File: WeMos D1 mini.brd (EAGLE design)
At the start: 25.4 x 28.9 mm, 19 parts

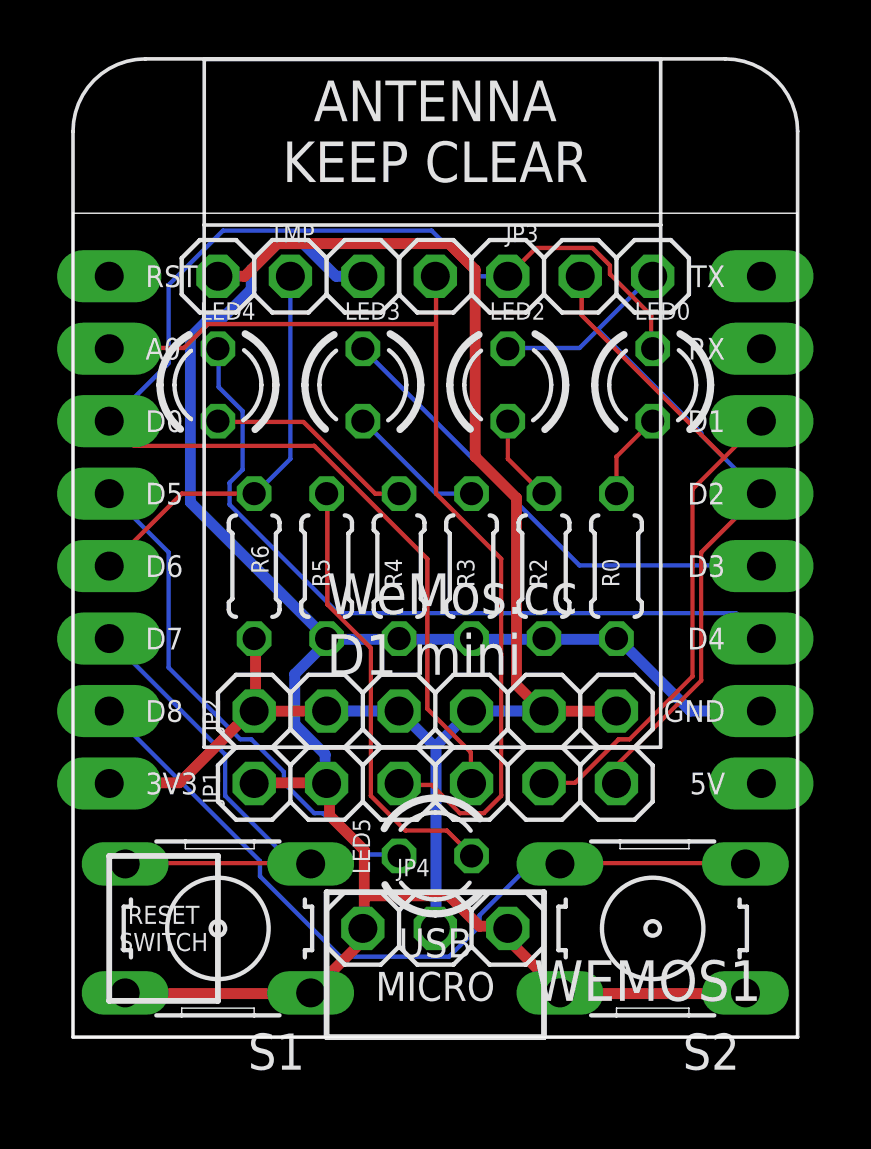
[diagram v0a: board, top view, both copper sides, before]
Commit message: Changed esp8266modules.lbr (esthetics)
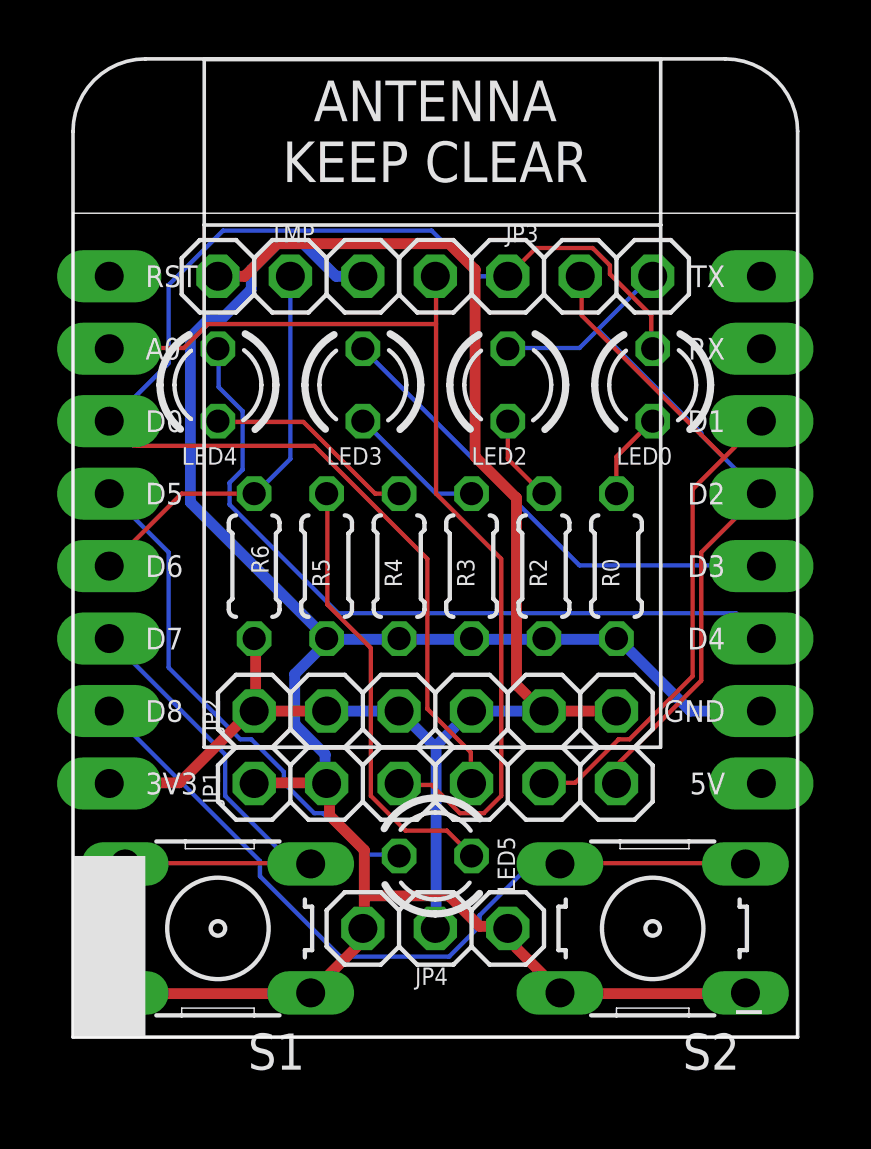
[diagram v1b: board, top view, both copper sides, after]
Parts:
- renumbered WEMOS1 to _
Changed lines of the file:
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@@
 </autorouter>
 <elements>
-<element name="WEMOS1" library="esp8266modules" package="WEMOS-D1-MINI" value="" x="11.43" y="19.05" smashed="yes">
+<element name="_" library="esp8266modules" package="WEMOS-D1-MINI" value="" x="11.43" y="19.05" smashed="yes">
 <attribute name="NAME" x="24.13" y="1.27" size="1.4224" layer="25" align="bottom-right"/>
 </element>
@@
 </element>
 <element name="LED0" library="led" library_urn="urn:adsk.eagle:library:259" package="LED3MM" package3d_urn="urn:adsk.eagle:package:15797/1" value="" x="20.32" y="22.86" smashed="yes" rot="R270">
-<attribute name="NAME" x="19.685" y="25.146" size="0.6096" layer="25" ratio="10"/>
+<attribute name="NAME" x="19.05" y="20.066" size="0.6096" layer="25" ratio="10"/>
 <attribute name="VALUE" x="18.669" y="20.955" size="1.27" layer="27" ratio="10" rot="R270"/>
 </element>
 <element name="LED2" library="led" library_urn="urn:adsk.eagle:library:259" package="LED3MM" package3d_urn="urn:adsk.eagle:package:15797/1" value="" x="15.24" y="22.86" smashed="yes" rot="R270">
-<attribute name="NAME" x="14.605" y="25.146" size="0.6096" layer="25" ratio="10"/>
+<attribute name="NAME" x="13.97" y="20.066" size="0.6096" layer="25" ratio="10"/>
 <attribute name="VALUE" x="13.589" y="20.955" size="1.27" layer="27" ratio="10" rot="R270"/>
 </element>
 <element name="LED3" library="led" library_urn="urn:adsk.eagle:library:259" package="LED3MM" package3d_urn="urn:adsk.eagle:package:15797/1" value="" x="10.16" y="22.86" smashed="yes" rot="R270">
-<attribute name="NAME" x="9.525" y="25.146" size="0.6096" layer="25" ratio="10"/>
+<attribute name="NAME" x="8.89" y="20.066" size="0.6096" layer="25" ratio="10"/>
 <attribute name="VALUE" x="8.509" y="20.955" size="1.27" layer="27" ratio="10" rot="R270"/>
 </element>
@@
 </element>
 <element name="LED4" library="led" library_urn="urn:adsk.eagle:library:259" package="LED3MM" package3d_urn="urn:adsk.eagle:package:15797/1" value="" x="5.08" y="22.86" smashed="yes" rot="R270">
-<attribute name="NAME" x="4.445" y="25.146" size="0.6096" layer="25" ratio="10"/>
+<attribute name="NAME" x="3.81" y="20.066" size="0.6096" layer="25" ratio="10"/>
 <attribute name="VALUE" x="3.429" y="20.955" size="1.27" layer="27" ratio="10" rot="R270"/>
 </element>
@@
 </element>
 <element name="LED5" library="led" library_urn="urn:adsk.eagle:library:259" package="LED3MM" package3d_urn="urn:adsk.eagle:package:15797/1" value="" x="12.7" y="6.35" smashed="yes">
-<attribute name="NAME" x="10.414" y="5.715" size="0.6096" layer="25" ratio="10" rot="R90"/>
+<attribute name="NAME" x="15.494" y="5.08" size="0.6096" layer="25" ratio="10" rot="R90"/>
 <attribute name="VALUE" x="14.605" y="4.699" size="1.27" layer="27" ratio="10"/>
 </element>
@@
 </element>
 <element name="JP4" library="pinhead_v2" package="1X03/OCT" value="" x="12.7" y="3.81" smashed="yes">
-<attribute name="NAME" x="11.3538" y="5.6388" size="0.6096" layer="25" ratio="10"/>
+<attribute name="NAME" x="11.9888" y="1.8288" size="0.6096" layer="25" ratio="10"/>
 <attribute name="VALUE" x="8.89" y="0.635" size="1.27" layer="27"/>
 </element>
@@
 <signals>
 <signal name="VCC" class="1">
-<contactref element="WEMOS1" pad="3V3"/>
+<contactref element="_" pad="3V3"/>
 <contactref element="TMP" pad="1"/>
 <contactref element="R6" pad="2"/>
@@
 <contactref element="S1" pad="1"/>
 <contactref element="S1" pad="2"/>
-<contactref element="WEMOS1" pad="GND"/>
+<contactref element="_" pad="GND"/>
 <contactref element="S2" pad="2"/>
 <contactref element="S2" pad="1"/>
@@
 </signal>
 <signal name="D5">
-<contactref element="WEMOS1" pad="D5"/>
+<contactref element="_" pad="D5"/>
 <contactref element="LED5" pad="A"/>
 <wire x1="10.2108" y1="6.4008" x2="11.43" y2="6.4008" width="0.1524" layer="16"/>
@@
 </signal>
 <signal name="D6">
-<contactref element="WEMOS1" pad="D6"/>
+<contactref element="_" pad="D6"/>
 <contactref element="R6" pad="1"/>
 <contactref element="TMP" pad="2"/>
@@
 </signal>
 <signal name="D7">
-<contactref element="WEMOS1" pad="D7"/>
+<contactref element="_" pad="D7"/>
 <contactref element="S1" pad="3"/>
 <contactref element="S1" pad="4"/>
@@
 </signal>
 <signal name="D4">
-<contactref element="WEMOS1" pad="D4"/>
+<contactref element="_" pad="D4"/>
 <contactref element="LED4" pad="A"/>
 <wire x1="5.1054" y1="22.7838" x2="5.1054" y2="24.0792" width="0.1524" layer="16"/>
@@
 </signal>
 <signal name="D3">
-<contactref element="WEMOS1" pad="D3"/>
+<contactref element="_" pad="D3"/>
 <contactref element="LED3" pad="A"/>
 <wire x1="17.7546" y1="16.5354" x2="10.16" y2="24.13" width="0.1524" layer="16"/>
@@
 </signal>
 <signal name="D2">
-<contactref element="WEMOS1" pad="D2"/>
+<contactref element="_" pad="D2"/>
 <contactref element="LED2" pad="A"/>
 <contactref element="JP1" pad="6"/>
@@
 </signal>
 <signal name="D0">
-<contactref element="WEMOS1" pad="D0"/>
+<contactref element="_" pad="D0"/>
 <contactref element="JP1" pad="4"/>
 <contactref element="JP3" pad="2"/>
@@
 </signal>
 <signal name="A0">
-<contactref element="WEMOS1" pad="A0"/>
+<contactref element="_" pad="A0"/>
 <contactref element="JP1" pad="3"/>
 <contactref element="JP3" pad="1"/>
@@
 </signal>
 <signal name="D1">
-<contactref element="WEMOS1" pad="D1"/>
+<contactref element="_" pad="D1"/>
 <contactref element="JP1" pad="5"/>
 <contactref element="JP3" pad="3"/>
@@
 </signal>
 <signal name="D8">
-<contactref element="WEMOS1" pad="D8"/>
+<contactref element="_" pad="D8"/>
 <contactref element="S2" pad="3"/>
 <contactref element="S2" pad="4"/>

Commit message: esp8266modules.lbr pins changed to octagon shape
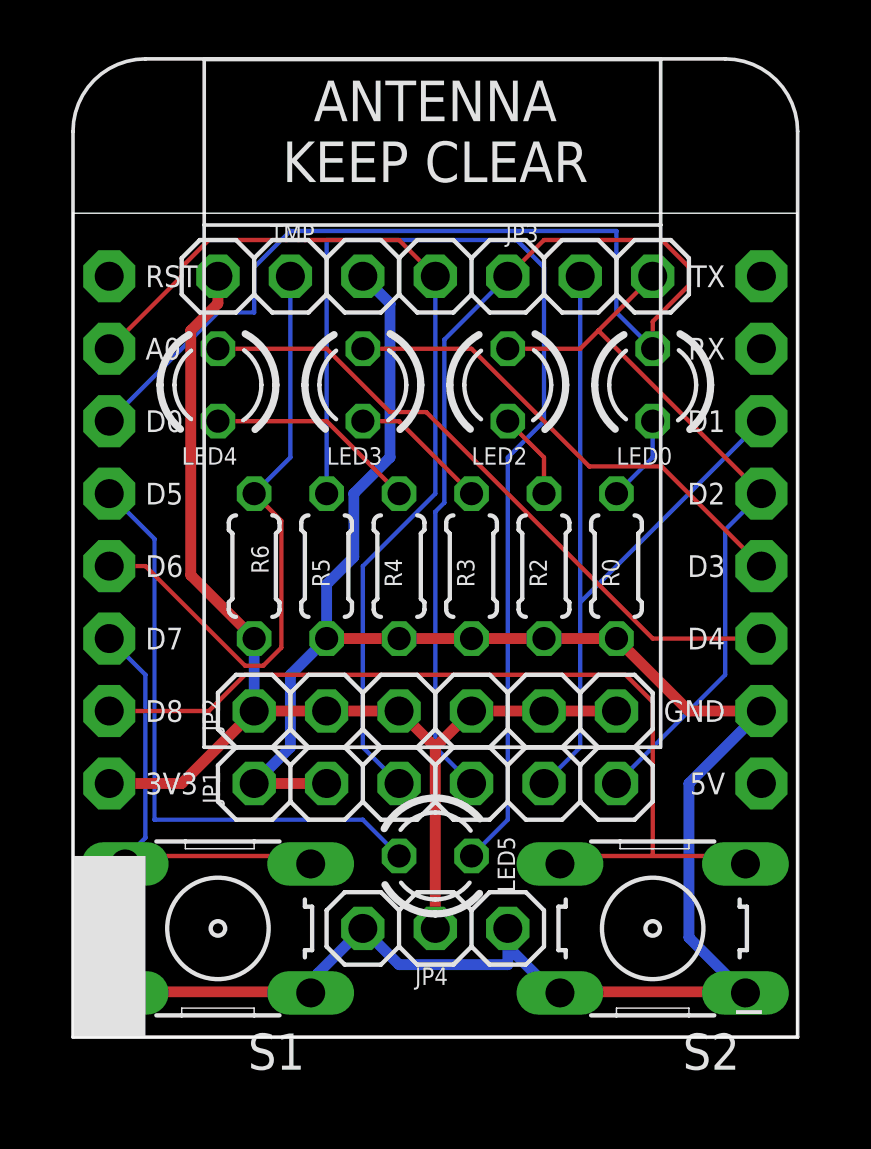
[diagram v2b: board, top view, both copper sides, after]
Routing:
- net N$5: track 15.7 -> 38.6 mm
- net VCC: track 55.2 -> 42.8 mm
- net D0: track 48.5 -> 56.1 mm
- net D6: track 14.3 -> 21.7 mm
- net D8: track 27.8 -> 32.3 mm
- net D4: track 26.6 -> 23.3 mm
- net D5: track 18.0 -> 21.2 mm
- net A0: track 35.3 -> 33.1 mm
- net D7: track 17.7 -> 15.6 mm
- net D1: track 25.2 -> 27.3 mm

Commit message: 1st prototype candidate 1
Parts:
- removed JP2: (no value), pinhead_v2:1X06/OCT
- removed JP4: (no value), pinhead_v2:1X03/OCT
- added GND: (no value), pinhead_v2:1X04/OCT
- added GND-VCC-GND: (no value), pinhead_v2:1X03/OCT
- added LED1: (no value), led:LED3MM
- added R1: (no value), resistor:0204/5
- added VCC: (no value), pinhead_v2:1X06/OCT
- JP1: device pinhead_v2:1X06/OCT -> pinhead_v2:1X07/OCT
- R6: value (none) -> 10K
- moved LED2 15.3 mm to (8.89, 8.89), turned to 0 degrees
- moved LED0 14.0 mm to (19.1, 8.89), turned to 0 degrees
- moved JP1 12.7 mm to (12.7, 21.6), turned to 180 degrees
- moved LED3 12.6 mm to (19.1, 14.0), turned to 0 degrees
- moved LED4 12.6 mm to (14.0, 14.0), turned to 0 degrees
- moved LED5 8.52 mm to (8.89, 14.0)
- moved R0 5.24 mm to (20.3, 21.6)
- moved R2 5.24 mm to (15.2, 21.6)
- moved R3 5.24 mm to (12.7, 21.6)
- moved R4 5.24 mm to (10.2, 21.6)
- moved R5 5.24 mm to (7.62, 21.6)
- moved R6 5.24 mm to (5.08, 21.6)
- moved S1 3.81 mm to (8.89, 3.81)
- moved S2 1.27 mm to (19.1, 3.81)
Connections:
- new net N$6: LED0.A, R0.1
- net A0: no longer JP1.3
- net D0: now also JP1.1, R0.2; no longer JP1.4, LED0.A
- net D1: now also JP1.2, R1.2; no longer JP1.5
- net D2: now also JP1.3, R2.2; no longer JP1.6, LED2.A
- net D3: now also JP1.4, R3.2; no longer LED3.A
- net D4: now also JP1.5, R4.2; no longer LED4.A
- net D5: now also JP1.6, R5.2; no longer LED5.A
- net D6: now also JP1.7
- net GND: now also GND-VCC-GND.1, GND-VCC-GND.3, GND.1, GND.2, GND.3, GND.4, LED0.K, LED1.K, LED2.K, LED3.K, LED4.K, LED5.K; no longer JP1.1, JP1.2, JP4.1, JP4.3, R0.1, R2.1, R3.1, R4.1, R5.1
- net N$1: now also LED5.A, R5.1; no longer LED0.K, R0.2
- net N$2: now also LED4.A, R4.1; no longer LED2.K, R2.2
- net N$3: now also LED3.A, R3.1; no longer LED3.K, R3.2
- net N$4: now also LED2.A, R2.1; no longer LED4.K, R4.2
- net N$5: now also LED1.A, R1.1; no longer LED5.K, R5.2
- net VCC: now also GND-VCC-GND.2, VCC.1, VCC.2, VCC.3, VCC.4, VCC.5, VCC.6; no longer JP2.1, JP2.2, JP2.3, JP2.4, JP2.5, JP2.6, JP4.2
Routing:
- net D0: track 56.1 -> 26.4 mm
- net N$5: track 38.6 -> 12.3 mm
- net A0: track 33.1 -> 12.5 mm
- net VCC: track 42.8 -> 60.9 mm, vias 0 -> 1
- net D1: track 27.3 -> 11.9 mm
- net GND: track 76.3 -> 87.8 mm
- net N$6: track 0.00 -> 11.3 mm
- net D5: track 21.2 -> 9.96 mm
- net D8: track 32.3 -> 23.3 mm
- net D6: track 21.7 -> 12.8 mm
- net D2: track 26.5 -> 17.9 mm
- net N$4: track 7.40 -> 13.4 mm
- net N$3: track 4.86 -> 8.04 mm
- net N$2: track 3.07 -> 6.16 mm
- net N$1: track 3.07 -> 5.90 mm
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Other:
- board size 25.4 x 28.9 mm -> 25.4 x 27.6 mm

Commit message: https://PCBs.io/share/z5oeo
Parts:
- removed S1, S2: (no value), switch-omron:B3F-10XX
- added BTN7: GND-D7, pinhead_v2:1X02/OCT
- added BTN8: GND-D8, pinhead_v2:1X02/OCT
- added RA0: 10K, resistor:0204/5
- added VCC-GND-5V: (no value), pinhead_v2:1X03/OCT
- JP1: device pinhead_v2:1X07/OCT -> pinhead_v2:1X08/OCT
- JP3: value (none) -> A0-D0-D1-D2-D3; device pinhead_v2:1X04/OCT -> pinhead_v2:1X05/OCT
- TMP: value (none) -> VCC-D6-GND
- moved GND-VCC-GND 23.4 mm to (6.35, 26.7), turned to 0 degrees
- moved TMP 20.7 mm to (3.81, 6.35)
- moved R2 1.27 mm to (16.5, 21.6)
- moved R3 1.27 mm to (14.0, 21.6)
- moved R5 1.27 mm to (8.89, 21.6)
- moved R0 1.27 mm to (21.6, 21.6)
- moved R1 1.27 mm to (19.1, 21.6)
- moved R4 1.27 mm to (11.4, 21.6)
- moved R6 1.27 mm to (6.35, 21.6)
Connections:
- new net 5V: VCC-GND-5V.3, _.5V
- net A0: now also RA0.2
- net D3: now also JP3.5
- net D6: no longer JP1.7
- net D7: now also BTN7.1, JP1.7; no longer S1.3, S1.4
- net D8: now also BTN8.1, JP1.8; no longer S2.3, S2.4
- net GND: now also BTN7.2, BTN8.2, RA0.1, VCC-GND-5V.2; no longer S1.1, S1.2, S2.1, S2.2
- net VCC: now also VCC-GND-5V.1
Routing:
- net D6: track 12.8 -> 28.5 mm
- net D8: track 23.3 -> 37.0 mm, vias 0 -> 2
- net VCC: track 60.9 -> 48.3 mm, vias 1 -> 0
- net D7: track 16.2 -> 28.8 mm, vias 0 -> 2
- net GND: track 87.8 -> 76.7 mm
- net D3: track 16.1 -> 22.6 mm
- net D2: track 17.9 -> 14.8 mm
- net 5V: track 0.00 -> 2.55 mm
- net N$5: track 12.3 -> 14.4 mm
- net N$3: track 8.04 -> 6.77 mm
- net D5: track 9.96 -> 11.2 mm
- net A0: track 12.5 -> 11.2 mm
- net N$4: track 13.4 -> 14.4 mm
- net D4: track 21.2 -> 20.6 mm
- net N$2: track 6.16 -> 5.61 mm
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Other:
- board size 25.4 x 27.6 mm -> 25.4 x 23.2 mm
